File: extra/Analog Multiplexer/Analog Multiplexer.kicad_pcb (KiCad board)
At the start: 2 copper layers, 50 x 70 mm, 11 parts, among them J1 Conn_01x05_Socket, J2 Conn_01x05_Socket, J3 Conn_01x05_Socket, J4 Conn_01x05_Socket, J5 Conn_01x05_Socket, J6 Conn_01x04_Socket, U1 TLV1117-33, U4 ADG729, U5 ADG729

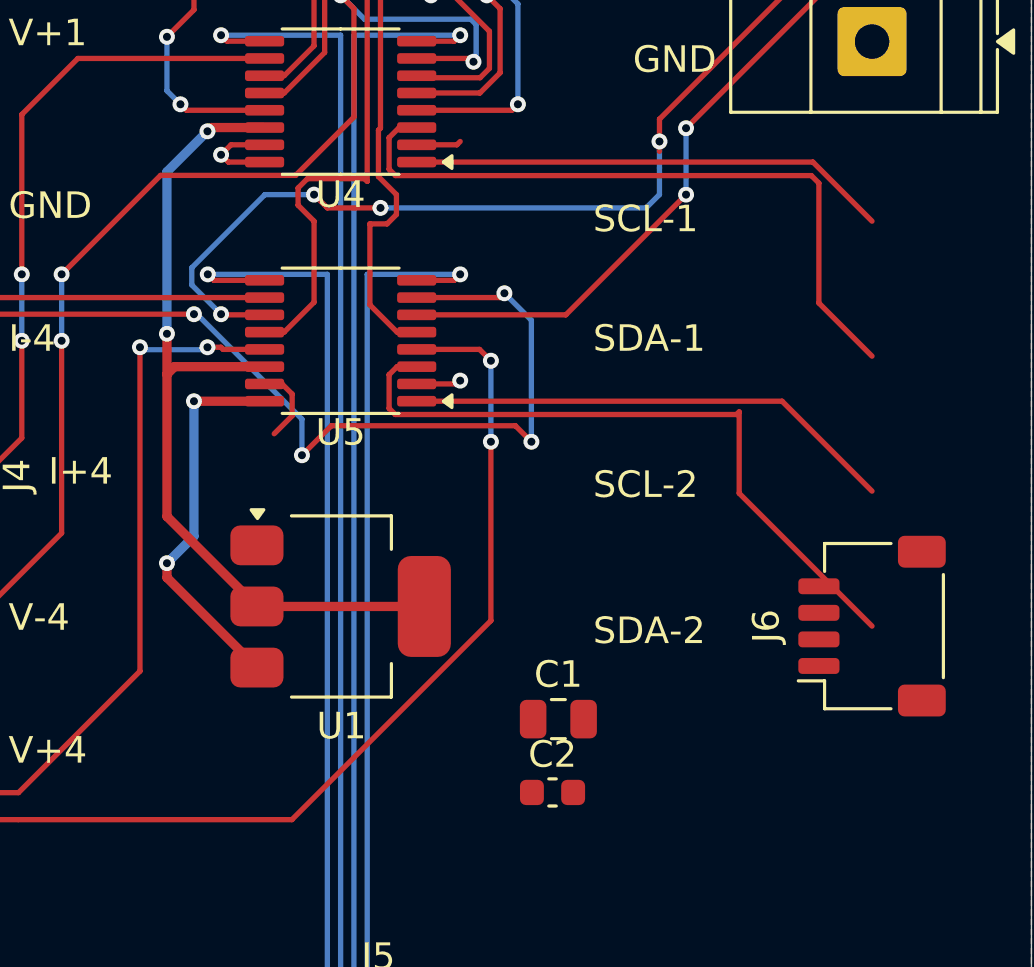
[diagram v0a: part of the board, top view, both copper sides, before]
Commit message: Bypass caps and I2C Header changed
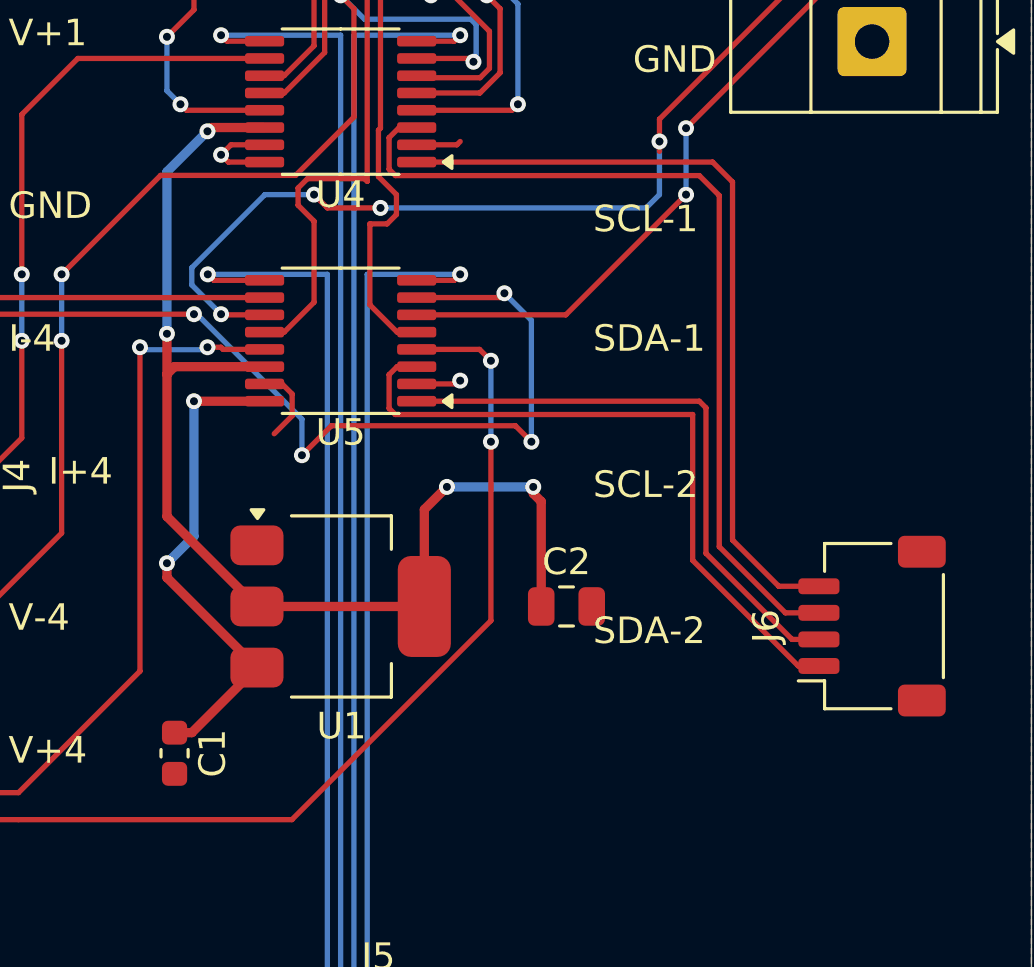
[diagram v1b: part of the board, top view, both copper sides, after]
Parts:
- C1: footprint Capacitor_SMD:C_0805_2012Metric -> Capacitor_SMD:C_0603_1608Metric
- C2: footprint Capacitor_SMD:C_0603_1608Metric -> Capacitor_SMD:C_0805_2012Metric
- moved C1 14.5 mm to (29.8, 62.5), turned to -90 degrees
- moved C2 7.02 mm to (44.5, 57.0)
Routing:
- net +3V3: track 32.2 -> 44.9 mm, vias 2 -> 4
- net /SCL-1: track 18.1 -> 29.6 mm
- net /SDA-1: track 26.1 -> 33.2 mm
- net VCC: track 14.5 -> 18.6 mm
- net /SCL-2: track 18.5 -> 22.1 mm

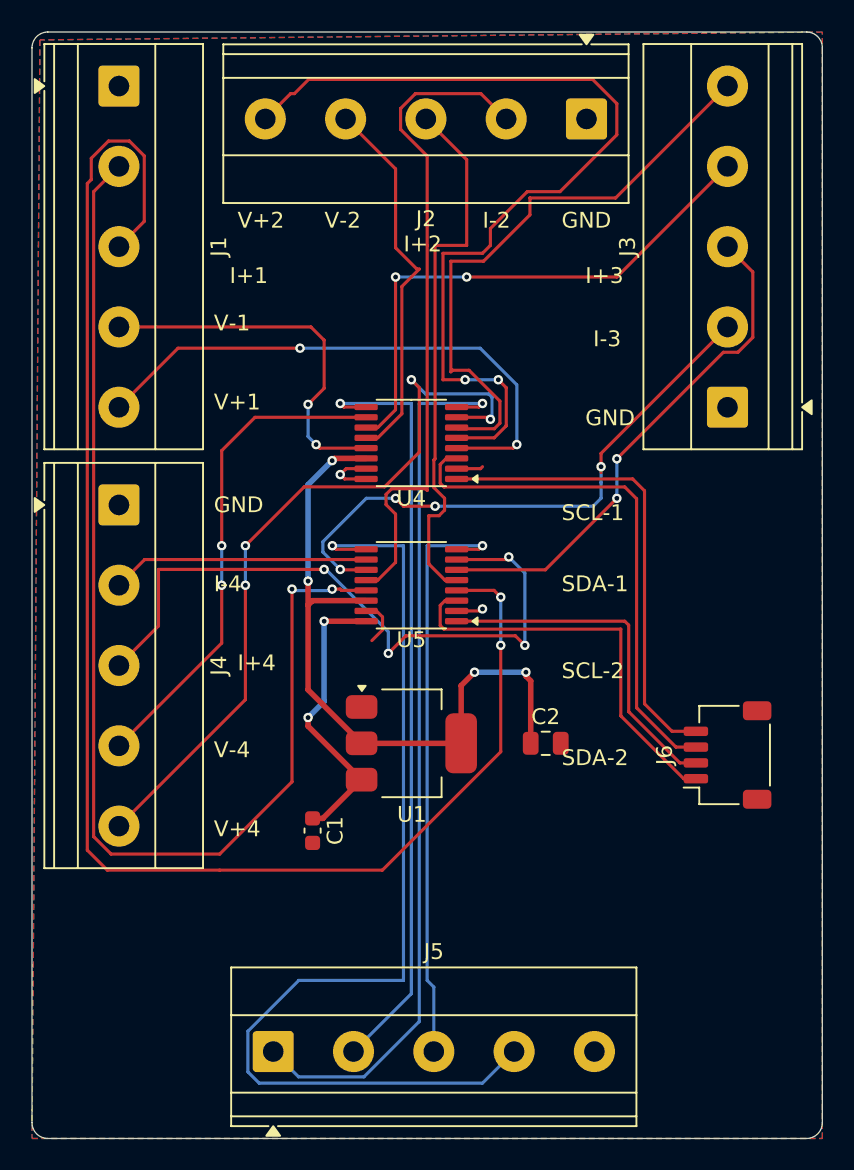
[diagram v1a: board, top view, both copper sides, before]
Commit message: Cleaned and added mounting holes
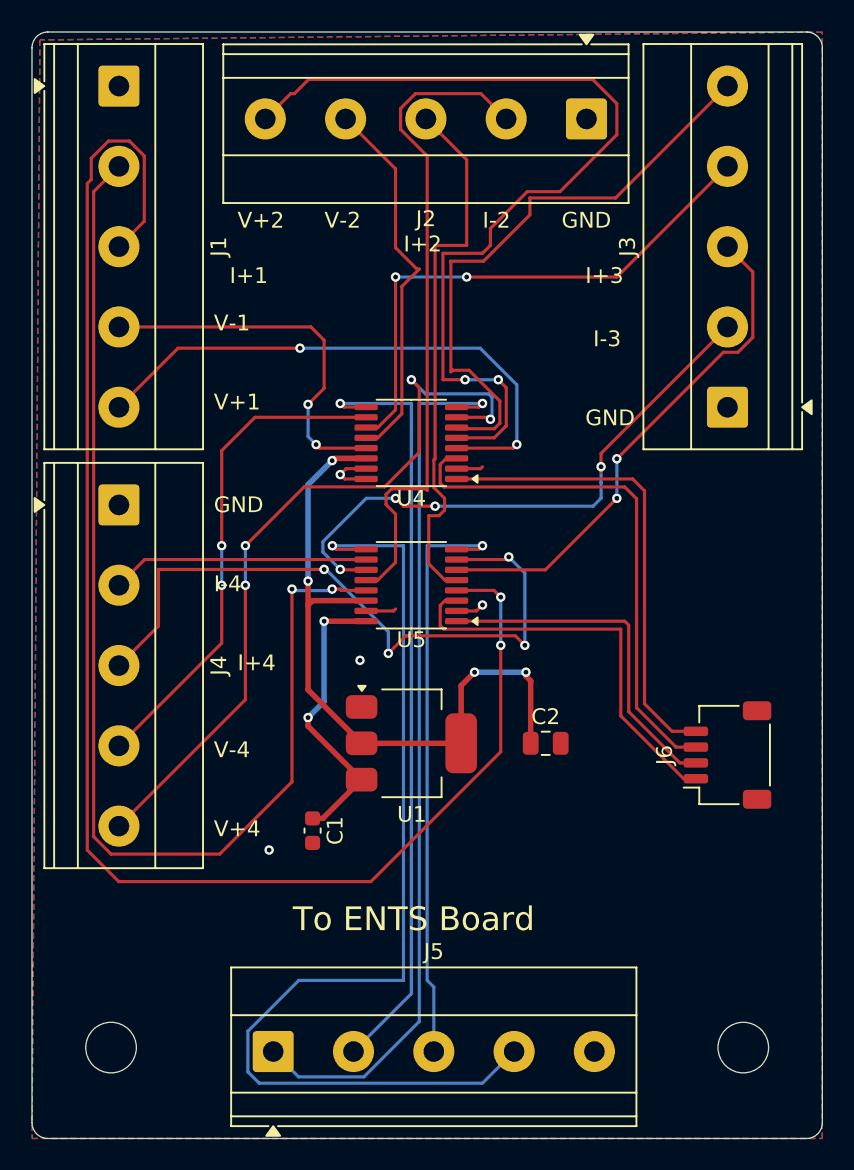
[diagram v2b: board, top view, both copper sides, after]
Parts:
- added H1: MountingHole, MountingHole:MountingHole_3.2mm_M3_ISO7380, F.Cu at (17.0, 76.2)
- added H2: MountingHole, MountingHole:MountingHole_3.2mm_M3_ISO7380, F.Cu at (57.0, 76.2)
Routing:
- net GND: track 9.89 -> 8.94 mm, vias 2 -> 4
- net /I+1: track 97.5 -> 98.1 mm
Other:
- board text added: "${TITLE} ${ISSUE_DATE} ${REVISION} ${COMPANY}"
- board text added: "Mounting holes 40mm apart"
- board text added: "To ENTS Board"
- board text removed: "SCL-1"
- board text removed: "SCL-2"
- board text removed: "SDA-1"
- board text removed: "SDA-2"
